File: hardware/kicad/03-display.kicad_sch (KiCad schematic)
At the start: 3 parts, among them J4 FPC-16P-0.5mm

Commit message: fix: close 3 of 4 flagged items from the docs audit; track the 4th
Follow-ups to the 2026-08-02 documentation audit (56dfae7):

- Display label: the generated sheet title and DS1 symbol value said
  "4.0in" while every design source is the 3.95" ILI9488 panel. Fixed in
  the generator (display.py), the KNOWN_MAPPINGS key in verify_bom_values,
  and the verify_schematic_pcb_sync docstring; schematic regenerated and
  the label-mismatch note removed from schematics.md.

- Speaker: footprint renamed Speaker-22mm -> Speaker-28mm across the
  generator and gates (the pads are driver-size-independent wire pads;
  the "22mm" was legacy from an early driver plan — the BOM part has been
  the 28mm driver all along). enclosure.scad documents the 22mm grille as
  the intentional radiating-cone opening for the 28mm frame. PCB and
  net-explorer data regenerated, vbench header re-derived.

- POLARITY_AUDIT.md brought back in line with the code: C2 row removed
  (component deleted in the R25 respin, section kept as marked history),
  U3 re-audited as SY8089AAAC C78988 (delta_row=0, family-formula 180deg,
  no waiver), the retired _JLCPCB_ROT_OVERRIDES quote replaced with the
  current _JLCPCB_ROT_DELTAS table, allowlist listing synced (U3 entry
  gone, LED2 red), stale action items closed (Q1/U4 datasheets are on
  disk). vbench findings page staleness note resolved accordingly.

- SD card-detect contradiction (bring-up docs vs verify_sd_interface vs
  Makefile naming of U6 pad 9) deliberately NOT resolved in prose:
  recorded as high-priority item 3 in docs/open-tasks.md for the
  pcb-engineer.

verify-all 93/93 green, verify_dfa 9/9, Docusaurus strict build passes.

Co-Authored-By: Claude Fable 5 <noreply@anthropic.com>
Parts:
- DS1: value ILI9488 4.0in 8080 -> ILI9488 3.95in 8080
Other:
- note added: "DISPLAY - ILI9488 3.95in 320x480"
- note removed: "DISPLAY - ILI9488 4.0in 320x480"
- title: Display - ILI9488 4.0in 8080 Parallel -> Display - ILI9488 3.95in 8080 Parallel
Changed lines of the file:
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@@
   (paper "A3")
   (title_block
-    (title "Display - ILI9488 4.0in 8080 Parallel")
+    (title "Display - ILI9488 3.95in 8080 Parallel")
     (comment 1 "ESP32 Emu Turbo - Handheld Retro Console")
     (comment 2 "Generated by scripts/generate_schematics")
   )
-  (text "DISPLAY - ILI9488 4.0in 320x480" (at 30 25 0) (effects (font (size 5 5) bold) (justify left)))
+  (text "DISPLAY - ILI9488 3.95in 320x480" (at 30 25 0) (effects (font (size 5 5) bold) (justify left)))
   (text "8-bit 8080 parallel interface (mandatory for SNES emulation speed)" (at 30 33 0) (effects (font (size 2.54 2.54)) (justify left)))
-  (symbol (lib_id "emu:ST7796S_Module") (at 148.59 119.38 0) (unit 1) (exclude_from_sim no) (in_bom yes) (on_board yes) (dnp no) (property "Reference" "DS1" (at 148.59 100.86999999999999 0) (effects (font (size 1.27 1.27)))) (property "Value" "ILI9488 4.0in 8080" (at 148.59 137.89 0) (effects (font (size 1.27 1.27)))) (pin "1") (pin "2") (pin "3") (pin "4") (pin "5") (pin "6") (pin "7") (pin "8") (pin "9") (pin "10") (pin "11") (pin "12") (pin "13") (pin "14") (pin "15") (pin "16") (instances (project "esp32-emu-turbo" (path "/00000004-cafe-4000-8000-000000000004" (reference "DS1") (unit 1)) (path "/00000001-cafe-4000-8000-000000000001/00000004-cafe-4000-8000-000000000004" (reference "DS1") (unit 1)))))
+  (symbol (lib_id "emu:ST7796S_Module") (at 148.59 119.38 0) (unit 1) (exclude_from_sim no) (in_bom yes) (on_board yes) (dnp no) (property "Reference" "DS1" (at 148.59 100.86999999999999 0) (effects (font (size 1.27 1.27)))) (property "Value" "ILI9488 3.95in 8080" (at 148.59 137.89 0) (effects (font (size 1.27 1.27)))) (pin "1") (pin "2") (pin "3") (pin "4") (pin "5") (pin "6") (pin "7") (pin "8") (pin "9") (pin "10") (pin "11") (pin "12") (pin "13") (pin "14") (pin "15") (pin "16") (instances (project "esp32-emu-turbo" (path "/00000004-cafe-4000-8000-000000000004" (reference "DS1") (unit 1)) (path "/00000001-cafe-4000-8000-000000000001/00000004-cafe-4000-8000-000000000004" (reference "DS1") (unit 1)))))
   (global_label "+3V3" (shape input) (at 118.11 104.14 0) (effects (font (size 1.27 1.27))) (property "Intersheetrefs" "" (at 0 0 0) (effects (font (size 1.27 1.27)) hide)))
   (wire (pts (xy 118.11 104.14) (xy 138.43 104.14)) (stroke (width 0) (type default)))

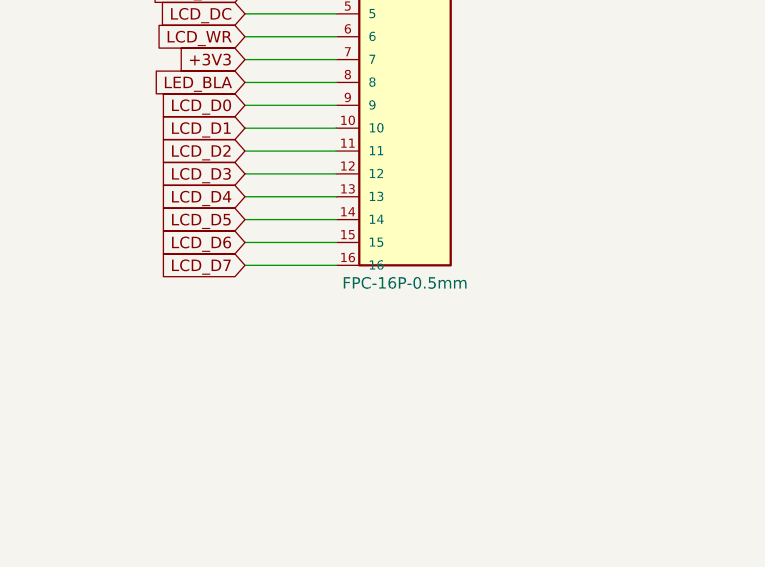
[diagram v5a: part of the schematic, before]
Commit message: cleanups: verify R14's DNP, name J4's real part, stop reporting (0,0,0,0)
Three from the "known fix, known reason they are open" list.

R14 — verified rather than trusted. Four sources, none of them each other:
the BOM's 10k 0805 line reads "R3,R4,...,R13,R15" quantity 12, so R14 is
the one gap in a contiguous run; the CPL has 0 of 94 rows for it; the
footprint IS placed on the board but pad 2 carries NO NET while its
neighbours R13.2 and R15.2 are both on +3V3, i.e. the pull-up leg is
deliberately unrouted; and the reason it must not be fitted is that R14
would pull BTN_L = GPIO45 = the VDD_SPI strapping pin up to +3V3, and
GPIO45 must be LOW at reset to select 3.3 V VDD_SPI, which the Octal PSRAM
requires. Recorded at EXCLUDED_REFS, where the exclusion is claimed.

J4 — the mapping was hiding a real disagreement, not a naming style. The
schematic value said "FPC-16P-0.5mm" while a 40-pin connector (C2856812)
is what gets soldered, and KNOWN_MAPPINGS taught verify_bom_values to
accept it. Value fixed at source to the BOM's own "FPC 40-pin 0.5mm Bottom
Contact"; the strings now match with no help and the entry is deleted. The
symbol still DRAWS 16 pins and should — only 16 of the 40 carry a signal,
that is a drawing simplification. Naming a 16-pin part was not.

verify_copper_clearance — (0,0,0,0) is a real coordinate on this board,
the bottom-left corner, so the fallback was not "no position", it was a
wrong one, and a reader had no way to tell them apart. _locate() degrades
now: true closest points, else a representative_point guaranteed inside
each geometry, else the bounding-box centres; approximated positions print
with a leading `~`. No path can return zeros. The three near-identical
report loops collapse into one formatter.

Gates: verify_bom_values 92/92 (mapping gone), verify_netlist_diff 4/4,
verify_copper_clearance 0 DANGER / 0 WARN, verify_dfa 9/9. Schematic
regenerated: 2 value strings changed, nothing else.

Co-Authored-By: Claude Fable 5 <noreply@anth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
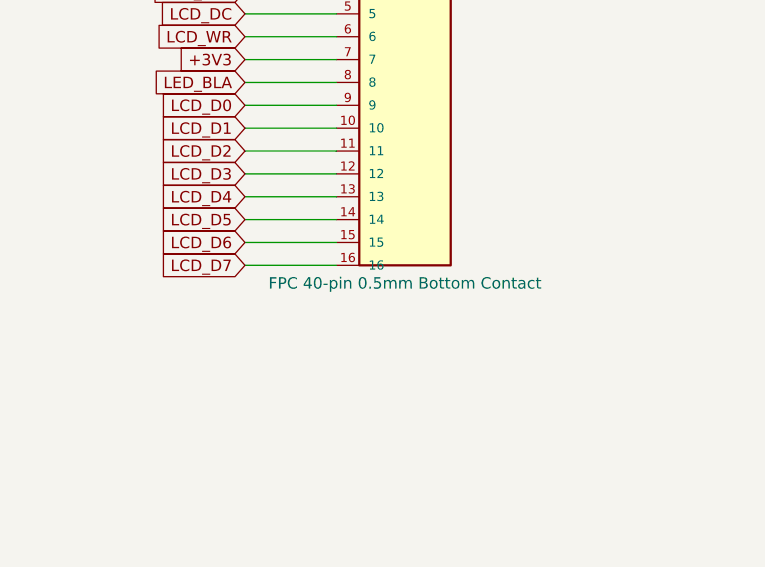
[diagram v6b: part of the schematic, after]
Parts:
- J4: value FPC-16P-0.5mm -> FPC 40-pin 0.5mm Bottom Contact
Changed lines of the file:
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@@
   (text "FPC RIBBON CONNECTOR (J4)" (at 245 95 0) (effects (font (size 2 2) bold) (justify left)))
   (text "(40P on PCB, 16 active signals shown)" (at 215 97 0) (effects (font (size 1.5 1.5)) (justify left)))
-  (symbol (lib_id "emu:FPC_16P") (at 260.35 119.38 0) (unit 1) (exclude_from_sim no) (in_bom yes) (on_board yes) (dnp no) (property "Reference" "J4" (at 260.35 97.06 0) (effects (font (size 1.27 1.27)))) (property "Value" "FPC-16P-0.5mm" (at 260.35 141.7 0) (effects (font (size 1.27 1.27)))) (pin "1") (pin "2") (pin "3") (pin "4") (pin "5") (pin "6") (pin "7") (pin "8") (pin "9") (pin "10") (pin "11") (pin "12") (pin "13") (pin "14") (pin "15") (pin "16") (instances (project "esp32-emu-turbo" (path "/00000004-cafe-4000-8000-000000000004" (reference "J4") (unit 1)) (path "/00000001-cafe-4000-8000-000000000001/00000004-cafe-4000-8000-000000000004" (reference "J4") (unit 1)))))
+  (symbol (lib_id "emu:FPC_16P") (at 260.35 119.38 0) (unit 1) (exclude_from_sim no) (in_bom yes) (on_board yes) (dnp no) (property "Reference" "J4" (at 260.35 97.06 0) (effects (font (size 1.27 1.27)))) (property "Value" "FPC 40-pin 0.5mm Bottom Contact" (at 260.35 141.7 0) (effects (font (size 1.27 1.27)))) (pin "1") (pin "2") (pin "3") (pin "4") (pin "5") (pin "6") (pin "7") (pin "8") (pin "9") (pin "10") (pin "11") (pin "12") (pin "13") (pin "14") (pin "15") (pin "16") (instances (project "esp32-emu-turbo" (path "/00000004-cafe-4000-8000-000000000004" (reference "J4") (unit 1)) (path "/00000001-cafe-4000-8000-000000000001/00000004-cafe-4000-8000-000000000004" (reference "J4") (unit 1)))))
   (global_label "+3V3" (shape input) (at 242.57 101.6 180) (effects (font (size 1.27 1.27))) (property "Intersheetrefs" "" (at 0 0 0) (effects (font (size 1.27 1.27)) hide)))
   (wire (pts (xy 252.73 101.6) (xy 242.57 101.6)) (stroke (width 0) (type default)))

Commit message: schematic: zero rendered text overlaps + real P-MOSFET artwork for Q1/Q2
The rendered sheets carried 75 text-on-text collisions the overlap gate
could not see: its model missed pin-number digits, KiCad's mirrored
field justification on 180-degree symbols, and global-label extents.
Root fixes in the generator:

- symbol() now places Reference/Value per part class: beside the body
  for two-pin verticals (R/C/L/Battery), stacked above for LEDs and the
  big ICs whose bottom pin numbers the old centred Value printed over,
  with per-call overrides where a zone is tight. On 180-rotated symbols
  the emitted justification is pre-mirrored, because KiCad flips it.
- Q1/Q2 get PMOS_SOT23 — same pin coordinates as the BAT54C symbol they
  were drawn with (wires and netlist untouched), but the artwork is now
  a P-MOSFET instead of a dual Schottky diode.
- Sheet-level relayouts: decoupling row on 02 spread to 11 mm pitch,
  menu-combo D1 zone on 06, FPC header on 03, PAM bias notes on 04,
  IP5306 KEY exit and the whole power-switch zone on 01.
- ESP32 module pin 41 name blanked — two "GND"s 2.54 mm apart printed
  into each other; number, type and net unchanged.

New gate: verify_schematic_render_overlaps.py exports each sheet to SVG
via kicad-cli and fails if any two DRAWN text runs intersect — ground
truth instead of a re-derived model (47 hits on the old sheet 01, 0
now). Wired into verify-all; dispatch mutation tests 14/14.

Netlist invariance: verify_netlist_diff 4/4, ERC clean at every
severity, schematic-PCB sync green. Website SVG/PDF re-rendered.

Co-Authored-By: Claude Fable 5 <noreply@anthropic.com>
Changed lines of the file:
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@@
   (text "DISPLAY - ILI9488 3.95in 320x480" (at 30 25 0) (effects (font (size 5 5) bold) (justify left)))
   (text "8-bit 8080 parallel interface (mandatory for SNES emulation speed)" (at 30 33 0) (effects (font (size 2.54 2.54)) (justify left)))
-  (symbol (lib_id "emu:ST7796S_Module") (at 148.59 119.38 0) (unit 1) (exclude_from_sim no) (in_bom yes) (on_board yes) (dnp no) (property "Reference" "DS1" (at 148.59 100.86999999999999 0) (effects (font (size 1.27 1.27)))) (property "Value" "ILI9488 3.95in 8080" (at 148.59 137.89 0) (effects (font (size 1.27 1.27)))) (pin "1") (pin "2") (pin "3") (pin "4") (pin "5") (pin "6") (pin "7") (pin "8") (pin "9") (pin "10") (pin "11") (pin "12") (pin "13") (pin "14") (pin "15") (pin "16") (instances (project "esp32-emu-turbo" (path "/00000004-cafe-4000-8000-000000000004" (reference "DS1") (unit 1)) (path "/00000001-cafe-4000-8000-000000000001/00000004-cafe-4000-8000-000000000004" (reference "DS1") (unit 1)))))
+  (symbol (lib_id "emu:ST7796S_Module") (at 148.59 119.38 0) (unit 1) (exclude_from_sim no) (in_bom yes) (on_board yes) (dnp no) (property "Reference" "DS1" (at 148.59 100.87 0) (effects (font (size 1.27 1.27)))) (property "Value" "ILI9488 3.95in 8080" (at 148.59 137.89 0) (effects (font (size 1.27 1.27)))) (pin "1") (pin "2") (pin "3") (pin "4") (pin "5") (pin "6") (pin "7") (pin "8") (pin "9") (pin "10") (pin "11") (pin "12") (pin "13") (pin "14") (pin "15") (pin "16") (instances (project "esp32-emu-turbo" (path "/00000004-cafe-4000-8000-000000000004" (reference "DS1") (unit 1)) (path "/00000001-cafe-4000-8000-000000000001/00000004-cafe-4000-8000-000000000004" (reference "DS1") (unit 1)))))
   (global_label "+3V3" (shape input) (at 118.11 104.14 0) (effects (font (size 1.27 1.27))) (property "Intersheetrefs" "" (at 0 0 0) (effects (font (size 1.27 1.27)) hide)))
   (wire (pts (xy 118.11 104.14) (xy 138.43 104.14)) (stroke (width 0) (type default)))
@@
   (global_label "LED_BLA" (shape bidirectional) (at 113.03 124.46 180) (effects (font (size 1.27 1.27))) (property "Intersheetrefs" "" (at 0 0 0) (effects (font (size 1.27 1.27)) hide)))
   (text "BL via R27 (FPC33)" (at 75.84 125.08 0) (effects (font (size 1.5 1.5)) (justify left)))
-  (symbol (lib_id "emu:R") (at 92.71 138.43 180) (unit 1) (exclude_from_sim no) (in_bom yes) (on_board yes) (dnp no) (property "Reference" "R27" (at 92.71 133.43 0) (effects (font (size 1.27 1.27)))) (property "Value" "20" (at 92.71 143.43 0) (effects (font (size 1.27 1.27)))) (pin "1") (pin "2") (instances (project "esp32-emu-turbo" (path "/00000004-cafe-4000-8000-000000000004" (reference "R27") (unit 1)) (path "/00000001-cafe-4000-8000-000000000001/00000004-cafe-4000-8000-000000000004" (reference "R27") (unit 1)))))
+  (symbol (lib_id "emu:R") (at 92.71 138.43 180) (unit 1) (exclude_from_sim no) (in_bom yes) (on_board yes) (dnp no) (property "Reference" "R27" (at 94.83 136.63 0) (effects (font (size 1.27 1.27)) (justify right))) (property "Value" "20" (at 94.83 140.23 0) (effects (font (size 1.27 1.27)) (justify right))) (pin "1") (pin "2") (instances (project "esp32-emu-turbo" (path "/00000004-cafe-4000-8000-000000000004" (reference "R27") (unit 1)) (path "/00000001-cafe-4000-8000-000000000001/00000004-cafe-4000-8000-000000000004" (reference "R27") (unit 1)))))
   (symbol (lib_id "emu:+5V") (at 92.71 129.54 0) (unit 1) (exclude_from_sim no) (in_bom no) (on_board no) (dnp no) (property "Reference" "#PWR002" (at 92.71 127.53999999999999 0) (effects (font (size 1.27 1.27)) hide)) (property "Value" "+5V" (at 92.71 131.54 0) (effects (font (size 1.27 1.27)) hide)) (pin "1") (instances (project "esp32-emu-turbo" (path "/00000004-cafe-4000-8000-000000000004" (reference "#PWR002") (unit 1)) (path "/00000001-cafe-4000-8000-000000000001/00000004-cafe-4000-8000-000000000004" (reference "#PWR002") (unit 1)))))
   (wire (pts (xy 92.71 129.54) (xy 92.71 134.62)) (stroke (width 0) (type default)))
@@
   (global_label "LCD_D7" (shape bidirectional) (at 182.88 121.92 0) (effects (font (size 1.27 1.27))) (property "Intersheetrefs" "" (at 0 0 0) (effects (font (size 1.27 1.27)) hide)))
   (text "GPIO11 (FPC24)" (at 198.16 122.54 0) (effects (font (size 1.5 1.5)) (justify left)))
-  (text "FPC RIBBON CONNECTOR (J4)" (at 245 95 0) (effects (font (size 2 2) bold) (justify left)))
-  (text "(40P on PCB, 16 active signals shown)" (at 215 97 0) (effects (font (size 1.5 1.5)) (justify left)))
+  (text "FPC RIBBON CONNECTOR (J4)" (at 235 92 0) (effects (font (size 2 2) bold) (justify left)))
+  (text "(40P on PCB, 16 active signals shown)" (at 235 95.5 0) (effects (font (size 1.5 1.5)) (justify left)))
   (symbol (lib_id "emu:FPC_16P") (at 260.35 119.38 0) (unit 1) (exclude_from_sim no) (in_bom yes) (on_board yes) (dnp no) (property "Reference" "J4" (at 260.35 97.06 0) (effects (font (size 1.27 1.27)))) (property "Value" "FPC 40-pin 0.5mm Bottom Contact" (at 260.35 141.7 0) (effects (font (size 1.27 1.27)))) (pin "1") (pin "2") (pin "3") (pin "4") (pin "5") (pin "6") (pin "7") (pin "8") (pin "9") (pin "10") (pin "11") (pin "12") (pin "13") (pin "14") (pin "15") (pin "16") (instances (project "esp32-emu-turbo" (path "/00000004-cafe-4000-8000-000000000004" (reference "J4") (unit 1)) (path "/00000001-cafe-4000-8000-000000000001/00000004-cafe-4000-8000-000000000004" (reference "J4") (unit 1)))))
   (global_label "+3V3" (shape input) (at 242.57 101.6 180) (effects (font (size 1.27 1.27))) (property "Intersheetrefs" "" (at 0 0 0) (effects (font (size 1.27 1.27)) hide)))
